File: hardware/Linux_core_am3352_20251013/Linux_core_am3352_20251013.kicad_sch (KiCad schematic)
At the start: 1 part, among them U1 AM3352BZCZ100

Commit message: update
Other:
- added sheet power_tps65217 (power_tps65217.kicad_sch)
- note added: "转换的电源需要引出"
- moved on the sheet: U1B
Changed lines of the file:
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@@
 	(generator_version "9.0")
 	(paper "A4")
+	(text "转换的电源需要引出"
+		(exclude_from_sim no)
+		(at 78.486 101.346 0)
+		(effects
+			(font
+				(size 1.27 1.27)
+			)
+		)
+	)
 	(symbol
 		(lib_id "My_Library:AM3352BZCZ100")
@@
 	(symbol
 		(lib_id "My_Library:AM3352BZCZ100")
-		(at 160.02 102.87 0)
+		(at 157.48 91.44 0)
 		(unit 2)
 		(exclude_from_sim no)
@@
 		(fields_autoplaced yes)
 		(property "Reference" "U1"
-			(at 160.02 26.67 0)
+			(at 157.48 15.24 0)
 			(effects
 				(font
@@
 		)
 		(property "Value" "AM3352BZCZ100"
-			(at 160.02 29.21 0)
+			(at 157.48 17.78 0)
 			(effects
 				(font
@@
 		)
 		(property "Footprint" "My_Library:ZCZ0324A"
-			(at 160.02 102.87 0)
+			(at 157.48 91.44 0)
 			(effects
 				(font
@@
 		)
 		(property "Datasheet" "https://www.ti.com/lit/gpn/am3352"
-			(at 160.02 102.87 0)
+			(at 157.48 91.44 0)
 			(effects
 				(font
@@
 		)
 		(property "Description" ""
-			(at 160.02 102.87 0)
+			(at 157.48 91.44 0)
 			(effects
 				(font
@@
 				)
 			)
+		)
+	)
+	(sheet
+		(at 66.04 119.38)
+		(size 21.59 34.29)
+		(exclude_from_sim no)
+		(in_bom yes)
+		(on_board yes)
+		(dnp no)
+		(fields_autoplaced yes)
+		(stroke
+			(width 0.1524)
+			(type solid)
+		)
+		(fill
+			(color 0 0 0 0.0000)
+		)
+		(property "Sheetname" "power_tps65217"
+			(at 66.04 118.6684 0)
+			(effects
+				(font
+					(size 1.27 1.27)
+				)
+				(justify left bottom)
+			)
+		)
+		(property "Sheetfile" "power_tps65217.kicad_sch"
+			(at 66.04 154.2546 0)
+			(effects
+				(font
+					(size 1.27 1.27)
+				)
+				(justify left top)
+			)
+		)
+		(instances
+			(project "Linux_core_am3352_20251013"
+				(path "/7fc27d12-54b0-4042-9bc1-38782b385460"
+					(page "3")
+				)
+			)

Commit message: update
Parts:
- removed U1: AM3352BZCZ100, My_Library:ZCZ0324A, symbol My_Library:AM3352BZCZ100
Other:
- added sheet am3352_b (am3352_b.kicad_sch)
- added sheet am3352_c (am3352_c.kicad_sch)
- added sheet am3352_d (am3352_d.kicad_sch)

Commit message: update
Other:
- sheet am3352_a ports: added DDR_CASn, DDR_CK, DDR_CKE, DDR_CKn, DDR_CSn0, DDR_DQM0, DDR_DQM1, DDR_DQS0, DDR_DQS1, DDR_DQSn0, DDR_DQSn1, DDR_ODT, DDR_RASn, DDR_RESETn, DDR_VREF, DDR_WEn, EXTINT_N, GPMC_ADV_ALE_N, GPMC_AD[0..15], GPMC_A[0..11], GPMC_BE0_CLE_N, GPMC_BE1_N, GPMC_CLK, GPMC_CS0_N, GPMC_CS1_N, GPMC_CS2_N, GPMC_CS3_N, GPMC_OEN_RE_N, GPMC_WAIT0, GPMC_WE_N, GPMC_WP_N, JTAG_EMU0, JTAG_EMU1, JTAG_TCK, JTAG_TDI, JTAG_TDO, JTAG_TMS, JTAG_TRST_N, MMC0_CLK, MMC0_CMD, MMC0_DAT0, MMC0_DAT1, MMC0_DAT2, MMC0_DAT3, PWRONRST_N, RTC_PORz, VDDSHV6, XDMA_EVENT_INTR0, XDMA_EVENT_INTR1; removed none
- sheet power_tps65217 ports: added PB_IN, PMIC_BAT1, PMIC_BAT2, PMIC_BATTEM_SENSE, PMIC_BAT_SENSE, PMIC_FB_WLED, PMIC_ISET1, PMIC_ISET2, PMIC_ISINK1, PMIC_ISINK2, PMIC_L4, PMIC_LDO_PGOOD, PMIC_LS1_OUT, PMIC_LS2_OUT, PMIC_MUX_IN, PMIC_MUX_OUT, PMIC_NINT, PMIC_NWAKEUP, PMIC_PGOOD, PMIC_POWER_EN, PMIC_SCL, PMIC_SDA, PMIC_SYS, PMIC_VLDO1, PMIC_VLDO2, USB_DC, VDDS_DDR, VDD_CORE, VDD_MPU, VIN; removed none

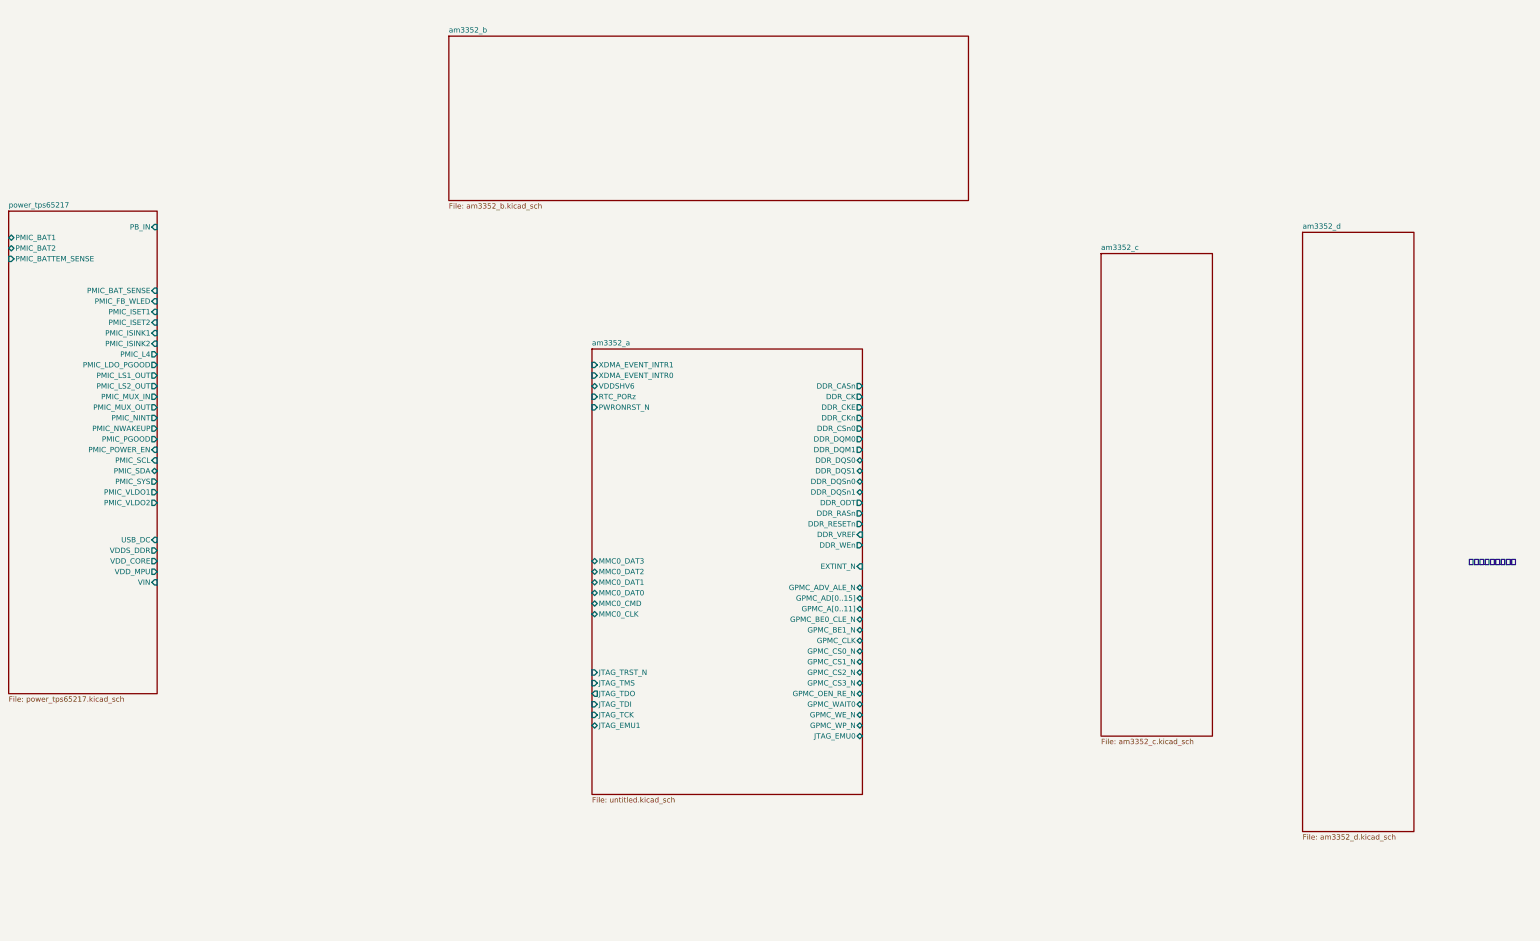
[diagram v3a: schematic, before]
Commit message: update schematic diagram
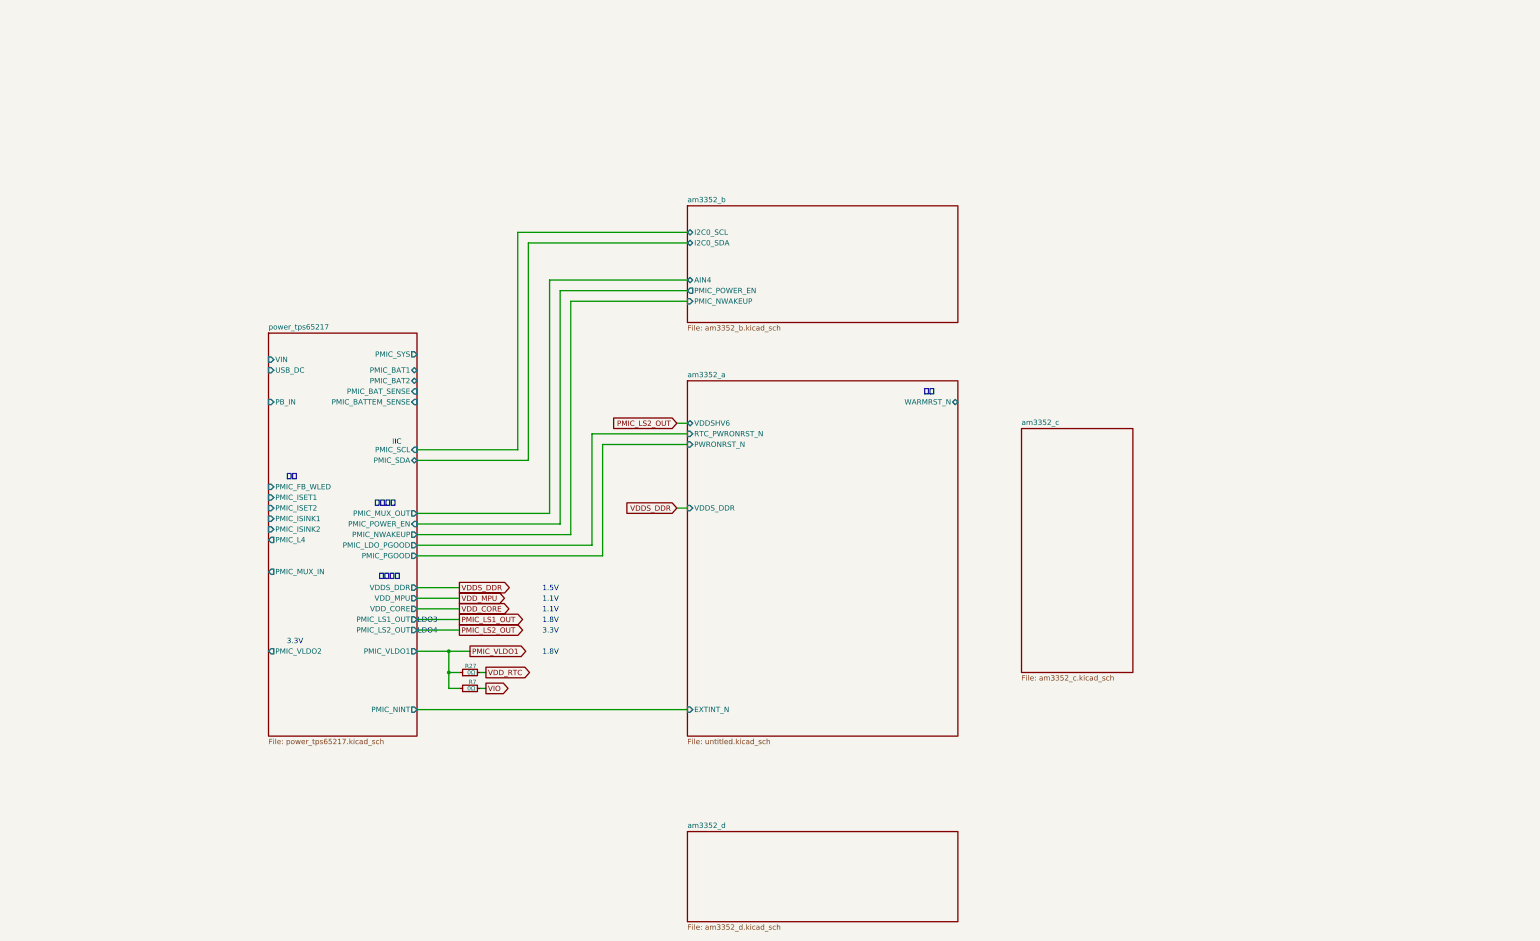
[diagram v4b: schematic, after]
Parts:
- added R27, R7: 0Ω, symbol Device:R_Small
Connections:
- new net PMIC_VLDO1: R27.1, R7.1
- new net VDD_RTC: R27.2
- new net VIO: R7.2
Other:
- sheet am3352_a ports: added RTC_PWRONRST_N, VDDS_DDR, WARMRST_N; removed DDR_CASn, DDR_CK, DDR_CKE, DDR_CKn, DDR_CSn0, DDR_DQM0, DDR_DQM1, DDR_DQS0, DDR_DQS1, DDR_DQSn0, DDR_DQSn1, DDR_ODT, DDR_RASn, DDR_RESETn, DDR_VREF, DDR_WEn, GPMC_ADV_ALE_N, GPMC_AD[0..15], GPMC_A[0..11], GPMC_BE0_CLE_N, GPMC_BE1_N, GPMC_CLK, GPMC_CS0_N, GPMC_CS1_N, GPMC_CS2_N, GPMC_CS3_N, GPMC_OEN_RE_N, GPMC_WAIT0, GPMC_WE_N, GPMC_WP_N, JTAG_EMU0, JTAG_EMU1, JTAG_TCK, JTAG_TDI, JTAG_TDO, JTAG_TMS, JTAG_TRST_N, MMC0_CLK, MMC0_CMD, MMC0_DAT0, MMC0_DAT1, MMC0_DAT2, MMC0_DAT3, RTC_PORz, XDMA_EVENT_INTR0, XDMA_EVENT_INTR1
- sheet am3352_b ports: added AIN4, I2C0_SCL, I2C0_SDA, PMIC_NWAKEUP, PMIC_POWER_EN; removed none
- note added: "1.1V"
- note added: "1.5V"
- note added: "1.8V"
- note added: "3.3V"
- note added: "IIC"
- note added: "LDO3"
- note added: "LDO4"
- note added: "内部电源"
- note added: "灯带"
- note added: "电源信号"
- note added: "重启"
- note removed: "转换的电源需要引出"
